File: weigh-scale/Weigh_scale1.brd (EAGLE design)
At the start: 93.6 x 33 mm, 6 parts

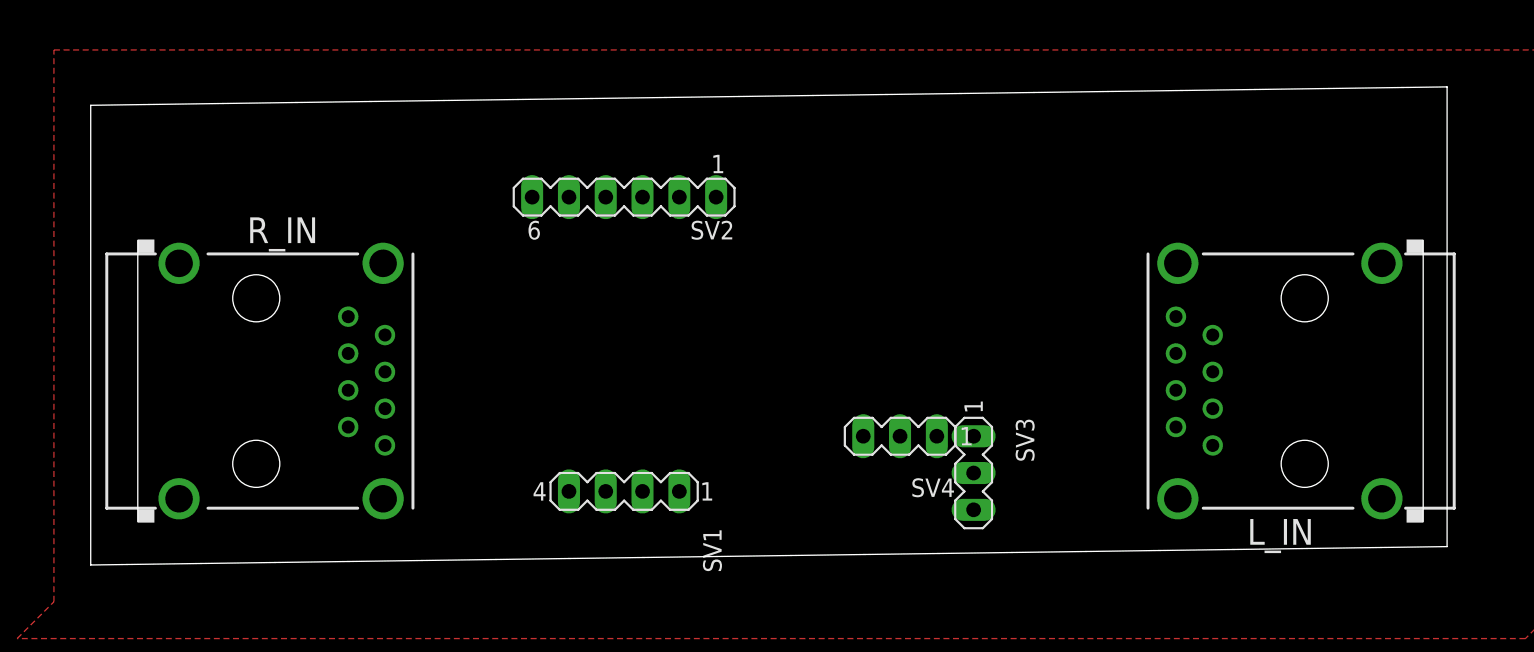
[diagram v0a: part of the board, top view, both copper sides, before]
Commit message: Weighing scale PCB v1.0 routed and linked to Fusion
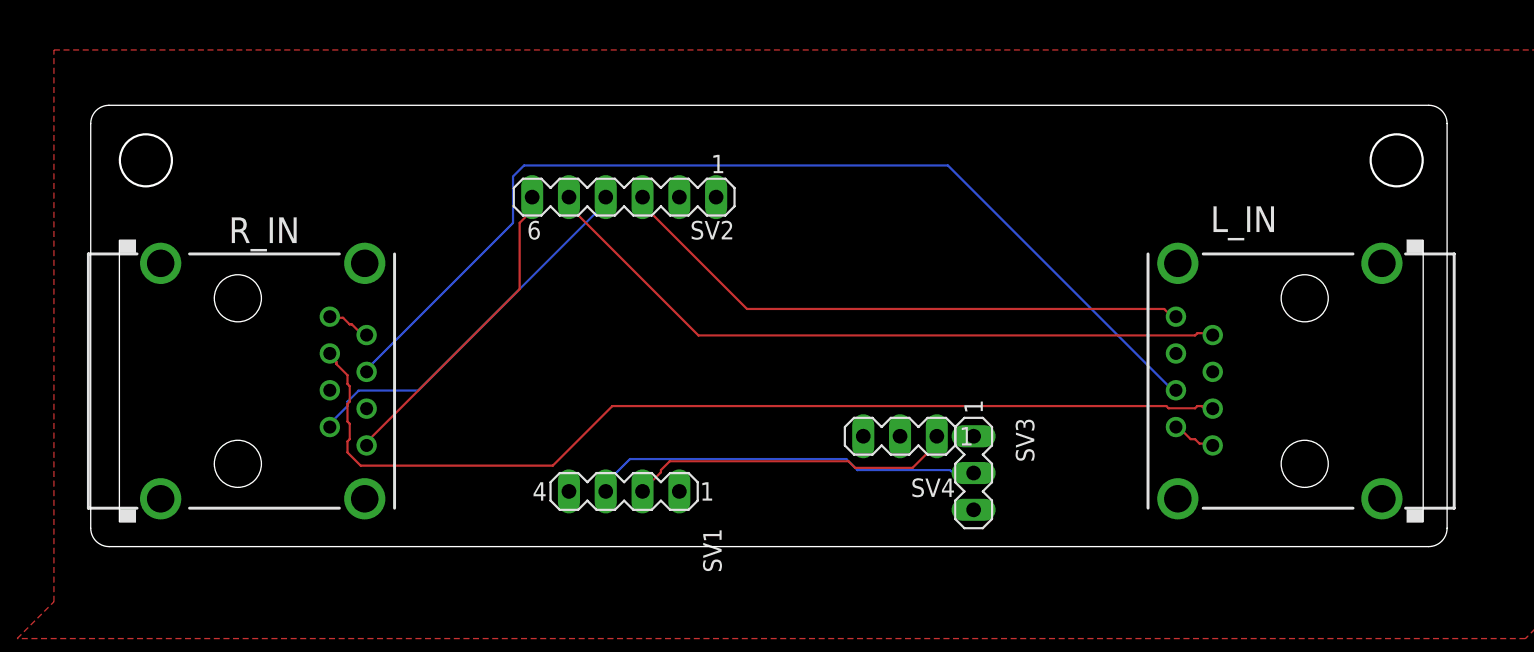
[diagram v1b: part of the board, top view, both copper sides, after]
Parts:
- moved R_IN 1.27 mm to (12.7, 12.7)
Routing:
- net N$8: track 0.00 -> 70.2 mm
- net N$7: track 0.00 -> 69.6 mm
- net E-: track 0.00 -> 49.0 mm
- net A+: track 0.00 -> 40.5 mm
- net HX_SCK_A2: track 0.00 -> 27.0 mm
- net A-: track 0.00 -> 26.2 mm
- net HX_DATA: track 0.00 -> 22.7 mm
- net E+: track 0.00 -> 21.9 mm
- net N$1: track 0.00 -> 3.13 mm
- net N$4: track 0.00 -> 3.12 mm
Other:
- board size 93.6 x 33 mm -> 93.6 x 30.5 mm
- board text added: "2/29/2020"
- board text added: "Cameron Fuller Jimmy He Jyotsna Joshi Sebastian Moruszewicz"
- board text added: "Mint Thia Tiffany Wang Jamie Xu"
- board text added: "WaggleNet"
- board text added: "Weighing Scale Baseboard"
- board text added: "rev-1.0"
